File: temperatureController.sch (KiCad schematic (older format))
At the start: 23 parts, among them J1 Barrel_Jack, J2 Screw_Terminal_01x02, J3 Conn_01x02_Male, J4 Conn_01x08_Male, Q1 Q_NMOS_GSD, U1 MAX7219

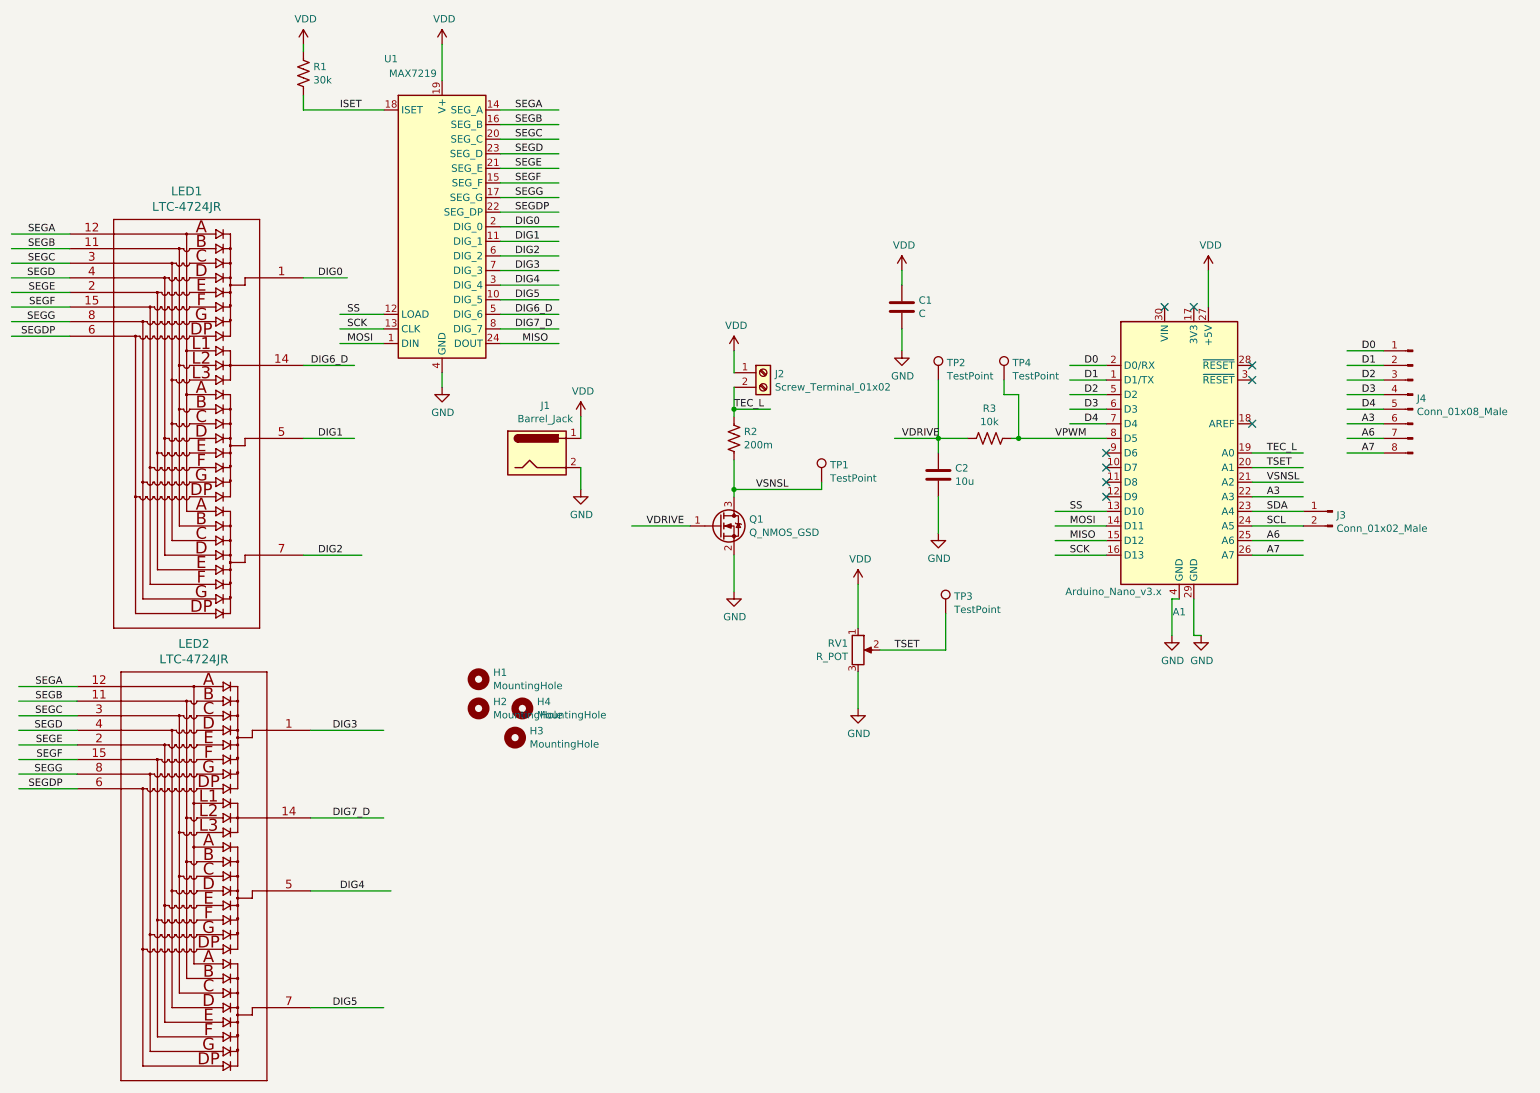
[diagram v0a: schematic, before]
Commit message: updated PCB to include 60x lower thermal resistance transistor. Added space for heatsink, rearranged some components. Added 6-pin connector for temperature readout
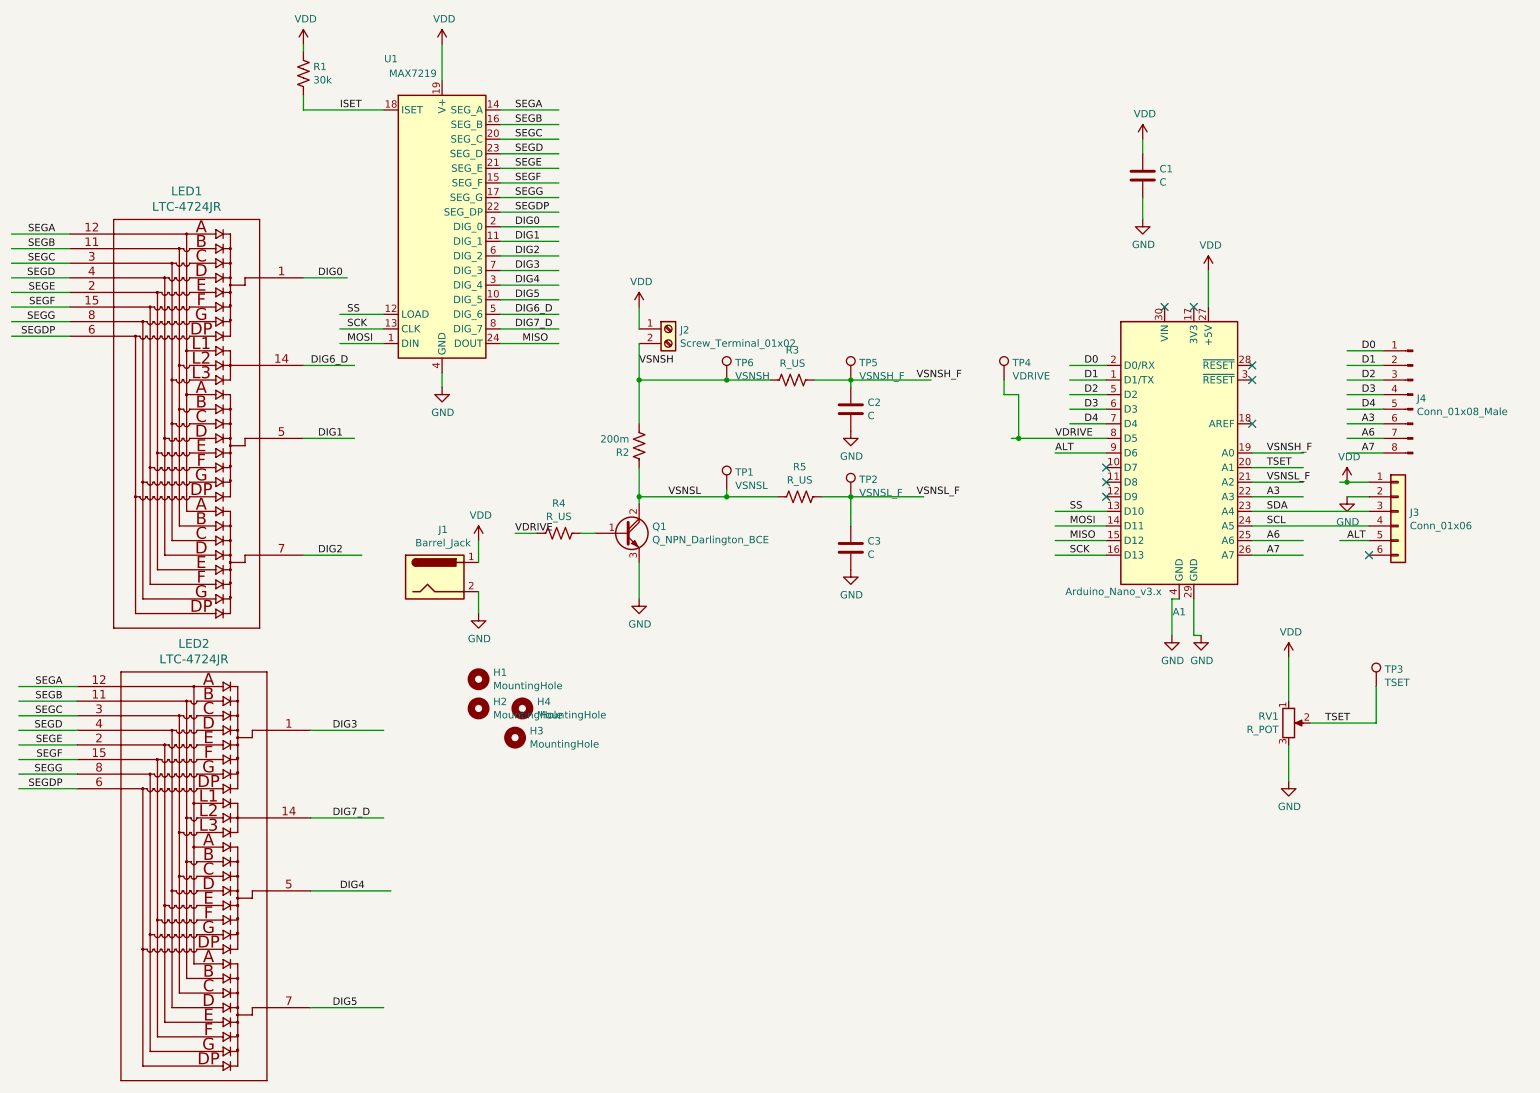
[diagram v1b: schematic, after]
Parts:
- removed J3: Conn_01x02_Male, Connector_PinHeader_2.54mm:PinHeader_1x02_P2.54mm_Vertical, symbol Connector:Conn_01x02_Male
- removed Q1: Q_NMOS_GSD, Package_TO_SOT_SMD:SOT-23, symbol Device:Q_NMOS_GSD
- added C3: C, Capacitor_SMD:C_0805_2012Metric_Pad1.15x1.40mm_HandSolder, symbol Device:C
- added J3: Conn_01x06, my_library_foot:S6B-XH-SM4-TB, symbol Connector_Generic:Conn_01x06
- added Q1: Q_NPN_Darlington_BCE, Package_TO_SOT_THT:TO-220-3_Vertical, symbol Device:Q_NPN_Darlington_BCE
- added R4, R5: R_US, Resistor_SMD:R_0805_2012Metric_Pad1.15x1.40mm_HandSolder, symbol Device:R_US
- added TP5: VSNSH_F, my_library_foot:TestPoint_Keystone_5000-5004_Miniature, symbol Connector:TestPoint
- added TP6: VSNSH, my_library_foot:TestPoint_Keystone_5000-5004_Miniature, symbol Connector:TestPoint
- C2: value 10u -> C
- R3: value 10k -> R_US
- TP1: value TestPoint -> VSNSL
- TP2: value TestPoint -> VSNSL_F
- TP3: value TestPoint -> TSET
- TP4: value TestPoint -> VDRIVE
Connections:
- net labels added: ALT, VSNSH, VSNSH_F, VSNSL_F
- net labels removed: TEC_L, VPWM
- wire segments 107 -> 116
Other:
- moved on the sheet: C1, J1, J2, R2, RV1, TP1, TP3

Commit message: updated README with features to make the thing readable
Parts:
- R4: value R_US -> 620R
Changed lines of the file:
@@
 P 4650 4050
 F 0 "R4" V 4445 4050 50  0000 C CNN
-F 1 "R_US" V 4536 4050 50  0000 C CNN
+F 1 "620R" V 4536 4050 50  0000 C CNN
 F 2 "Resistor_SMD:R_0805_2012Metric_Pad1.15x1.40mm_HandSolder" V 4690 4040 50  0001 C CNN
 F 3 "~" H 4650 4050 50  0001 C CNN

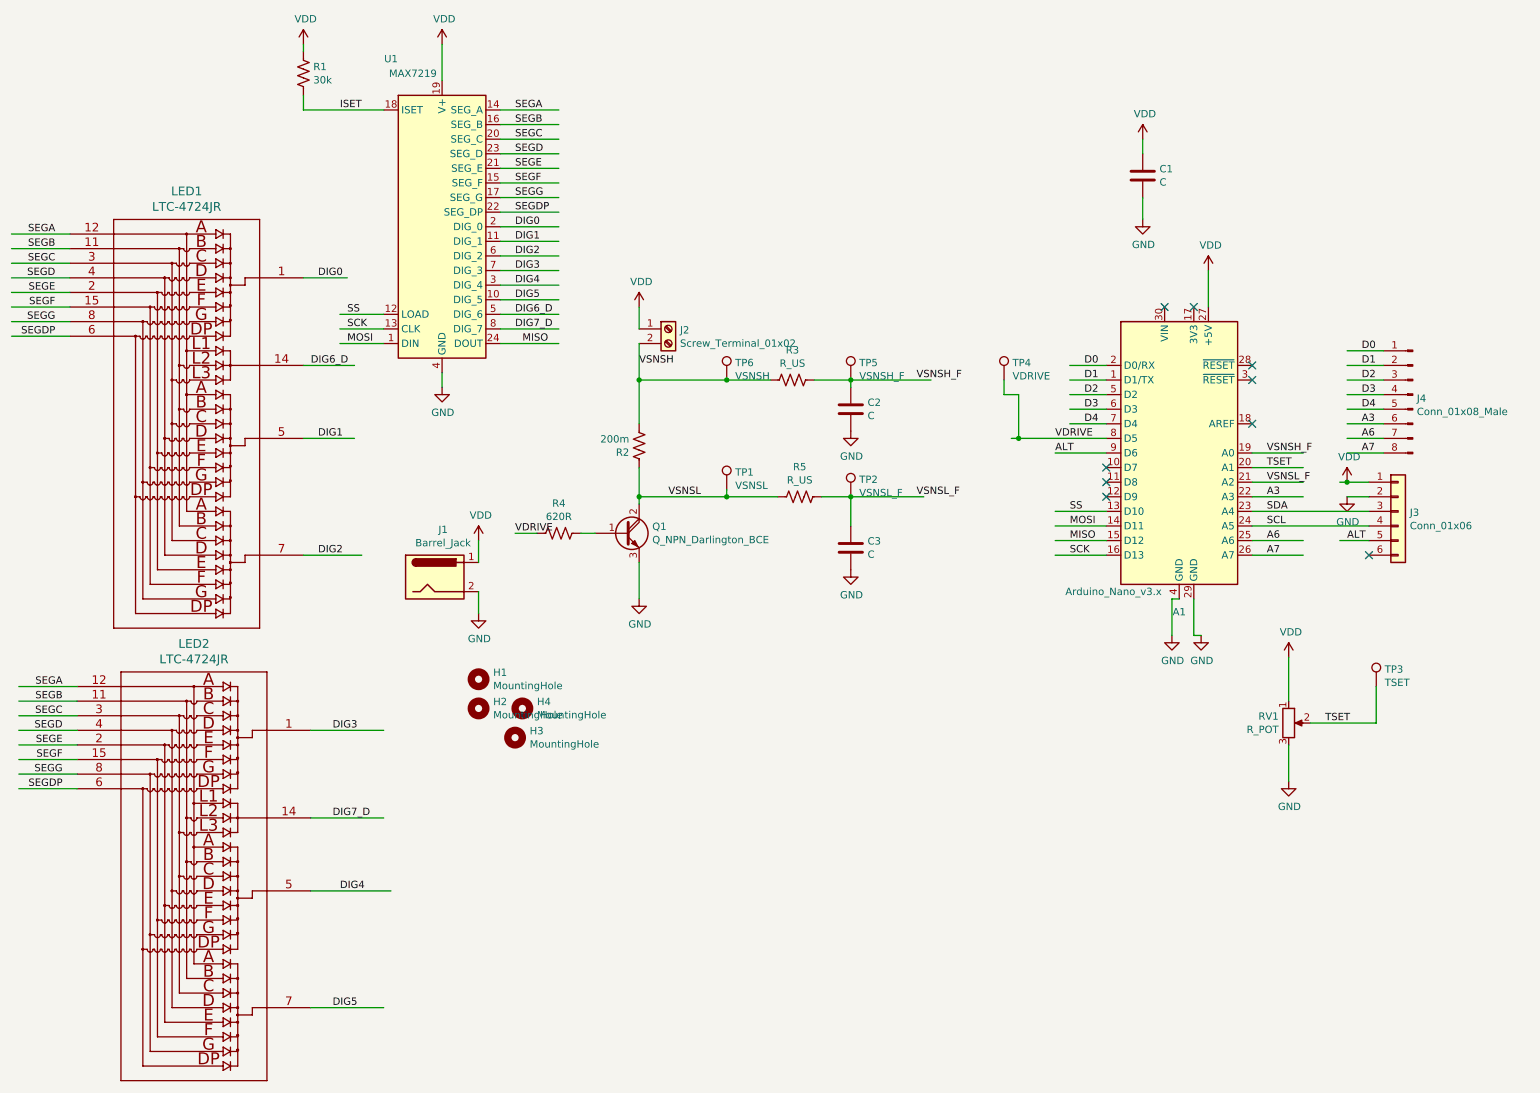
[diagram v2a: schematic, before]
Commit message: updated PCB with a relay, signal conditioning for sense resistor output. Ready to fabricate
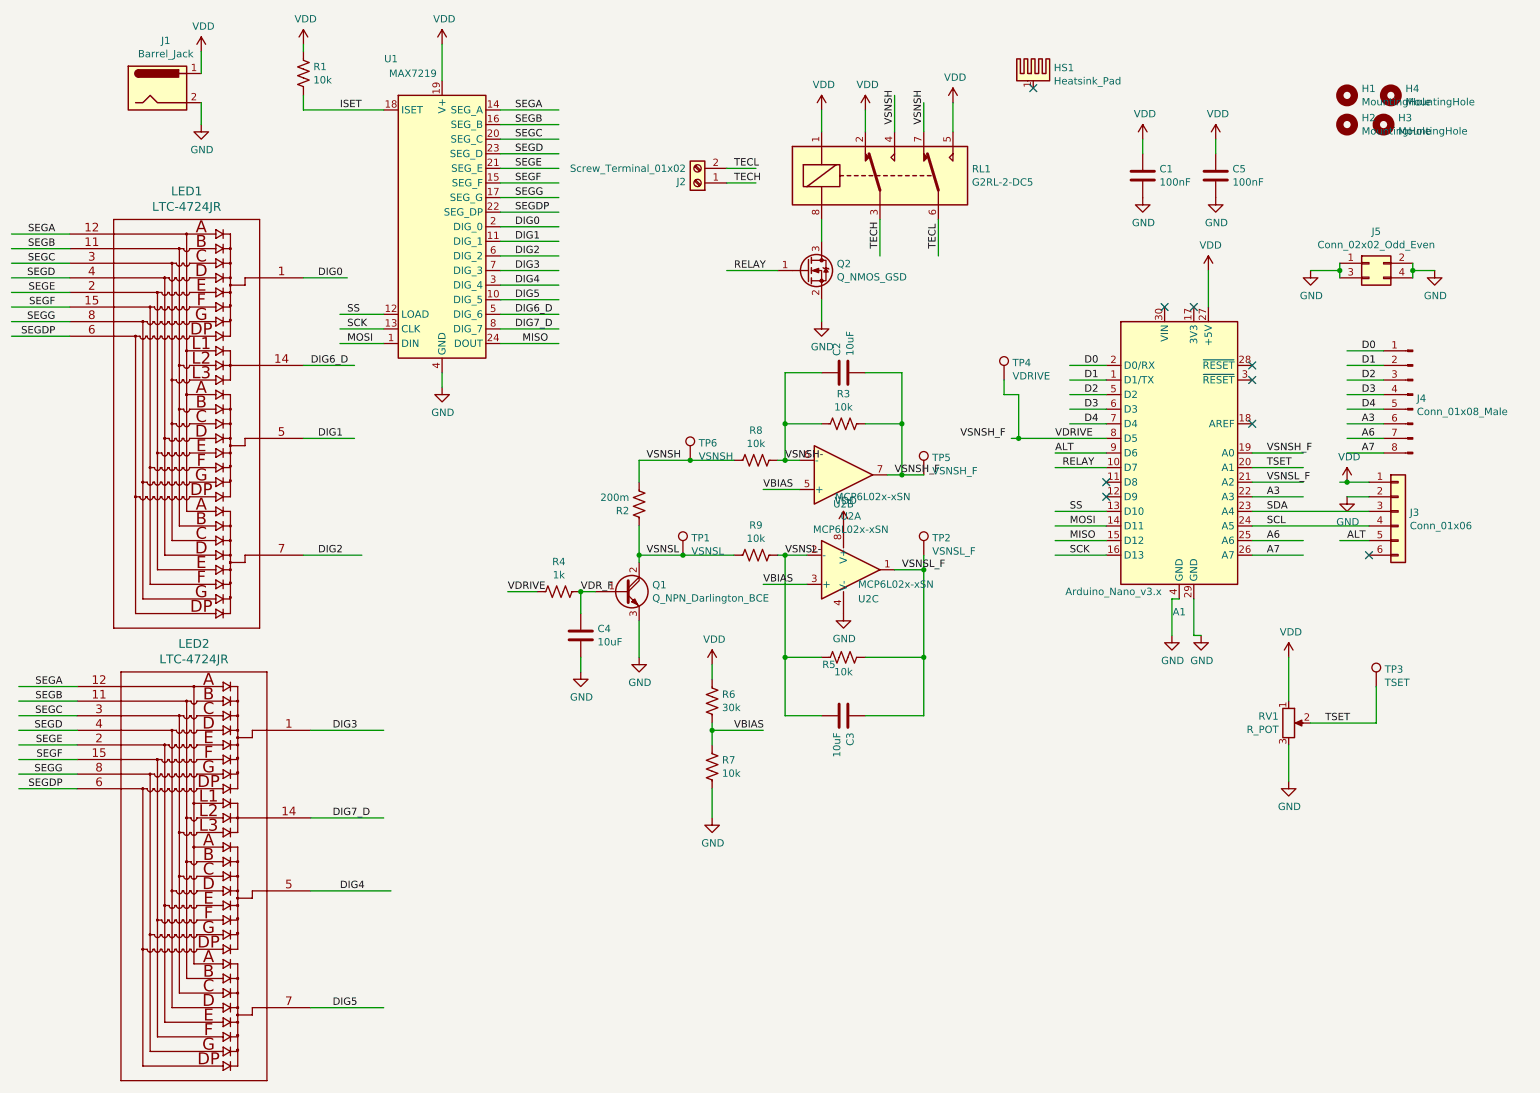
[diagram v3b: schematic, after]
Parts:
- added C4: 10uF, Capacitor_SMD:C_0805_2012Metric_Pad1.15x1.40mm_HandSolder, symbol Device:C
- added C5: 100nF, Capacitor_SMD:C_0805_2012Metric_Pad1.15x1.40mm_HandSolder, symbol Device:C
- added HS1: Heatsink_Pad, my_library_foot:heatsink, symbol Mechanical:Heatsink_Pad
- added J5: Conn_02x02_Odd_Even, Connector_PinHeader_2.54mm:PinHeader_2x02_P2.54mm_Vertical, symbol Connector_Generic:Conn_02x02_Odd_Even
- added Q2: Q_NMOS_GSD, Package_TO_SOT_SMD:SOT-323_SC-70_Handsoldering, symbol Device:Q_NMOS_GSD
- added R6: 30k, Resistor_SMD:R_0805_2012Metric_Pad1.15x1.40mm_HandSolder, symbol Device:R_US
- added R7, R8, R9: 10k, Resistor_SMD:R_0805_2012Metric_Pad1.15x1.40mm_HandSolder, symbol Device:R_US
- added RL1: G2RL-2-DC5, Relay_THT:Relay_DPDT_Omron_G2RL, symbol Relay:G2RL-2-DC5
- added U2: MCP6L02x-xSN, Package_SO:SOIC-8_3.9x4.9mm_P1.27mm, symbol Amplifier_Operational:MCP6L02x-xSN
- C1: value C -> 100nF
- C2, C3: value C -> 10uF
- R1: value 30k -> 10k
- R3, R5: value R_US -> 10k
- R4: value 620R -> 1k
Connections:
- net labels added: RELAY, TECH, TECL, VBIAS, VDR_F, VSNSH-, VSNSL-
- wire segments 116 -> 159
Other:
- moved on the sheet: C2, C3, H1, H2, H3, H4, J1, J2, Q1, R2, R3, R4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
